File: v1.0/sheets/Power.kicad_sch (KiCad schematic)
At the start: 28 parts, among them U6 XC6206P152MR, U7 XC6206P282MR, U8 SY8088AAC

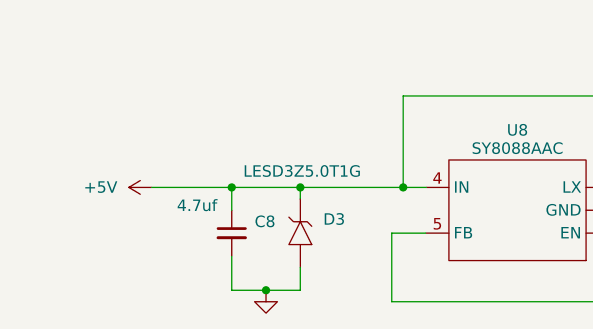
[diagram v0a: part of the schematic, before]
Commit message: V1.0 rework to match stm32u5xxxQ
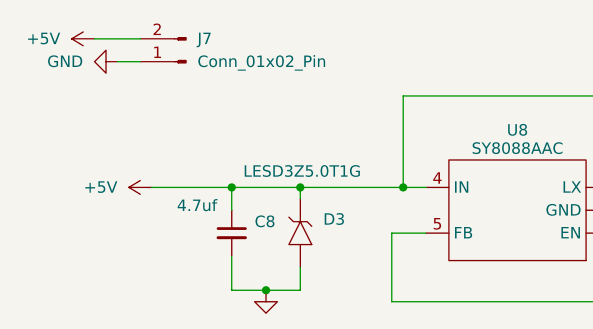
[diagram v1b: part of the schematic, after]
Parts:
- added J7: Conn_01x02_Pin, Connector_PinHeader_2.54mm:PinHeader_1x02_P2.54mm_Vertical, symbol Connector:Conn_01x02_Pin
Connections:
- net +5V: now also J7.2 (Pin_2)
- net GND: now also J7.1 (Pin_1)
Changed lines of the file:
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@@
 	(wire
 		(pts
+			(xy 17.78 15.24) (xy 22.86 15.24)
+		)
+		(stroke
+			(width 0)
+			(type default)
+		)
+	)
+	(wire
+		(pts
 			(xy 110.49 114.3) (xy 110.49 119.38)
 		)
@@
 	(wire
 		(pts
+			(xy 20.32 17.78) (xy 22.86 17.78)
+		)
+		(stroke
+			(width 0)
+			(type default)
+		)
+	)
+	(wire
+		(pts
 			(xy 24.13 31.75) (xy 33.02 31.75)
 		)
@@
 	)
 	(symbol
+		(lib_id "power:GND")
+		(at 20.32 17.78 270)
+		(unit 1)
+		(exclude_from_sim no)
+		(in_bom yes)
+		(on_board yes)
+		(dnp no)
+		(fields_autoplaced yes)
+		(property "Reference" "#PWR025"
+			(at 13.97 17.78 0)
+			(effects
+				(font
+					(size 1.27 1.27)
+				)
+				(hide yes)
+			)
+		)
+		(property "Value" "GND"
+			(at 16.51 17.7799 90)
+			(effects
+				(font
+					(size 1.27 1.27)
+				)
+				(justify right)
+			)
+		)
+		(property "Footprint" ""
+			(at 20.32 17.78 0)
+			(effects
+				(font
+					(size 1.27 1.27)
+				)
+				(hide yes)
+			)
+		)
+		(property "Datasheet" ""
+			(at 20.32 17.78 0)
+			(effects
+				(font
+					(size 1.27 1.27)
+				)
+				(hide yes)
+			)
+		)
+		(property "Description" "Power symbol creates a global label with name \"GND\" , ground"
+			(at 20.32 17.78 0)
+			(effects
+				(font
+					(size 1.27 1.27)
+				)
+				(hide yes)
+			)
+		)
+		(pin "1"
+		)
+		(instances
+			(project "v1.0"
+				(path "/4276d1e6-613e-409d-8b9b-79d391866e1c/7020a706-37b4-4081-90b2-84408c224fcc"
+					(reference "#PWR025")
+					(unit 1)
+				)
+			)
+		)
+	)
+	(symbol
 		(lib_id "Device:C_Small")
 		(at 121.92 36.83 0)
@@
 	)
 	(symbol
+		(lib_id "Connector:Conn_01x02_Pin")
+		(at 27.94 17.78 180)
+		(unit 1)
+		(exclude_from_sim no)
+		(in_bom yes)
+		(on_board yes)
+		(dnp no)
+		(fields_autoplaced yes)
+		(property "Reference" "J7"
+			(at 29.21 15.2399 0)
+			(effects
+				(font
+					(size 1.27 1.27)
+				)
+				(justify right)
+			)
+		)
+		(property "Value" "Conn_01x02_Pin"
+			(at 29.21 17.7799 0)
+			(effects
+				(font
+					(size 1.27 1.27)
+				)
+				(justify right)
+			)
+		)
+		(property "Footprint" "Connector_PinHeader_2.54mm:PinHeader_1x02_P2.54mm_Vertical"
+			(at 27.94 17.78 0)
+			(effects
+				(font
+					(size 1.27 1.27)
+				)
+				(hide yes)
+			)
+		)
+		(property "Datasheet" "~"
+			(at 27.94 17.78 0)
+			(effects
+				(font
+					(size 1.27 1.27)
+				)
+				(hide yes)
+			)
+		)
+		(property "Description" "Generic connector, single row, 01x02, script generated"
+			(at 27.94 17.78 0)
+			(effects
+				(font
+					(size 1.27 1.27)
+				)
+				(hide yes)
+			)
+		)
+		(pin "2"
+		)
+		(pin "1"
+		)
+		(instances
+			(project "v1.0"
+				(path "/4276d1e6-613e-409d-8b9b-79d391866e1c/7020a706-37b4-4081-90b2-84408c224fcc"
+					(reference "J7")
+					(unit 1)
+				)
+			)
+		)
+	)
+	(symbol
 		(lib_id "Grinreflex:MLF2012A1R5KT000")
 		(at 34.29 80.01 0)
@@
 					(unit 1)
 				)
+			)
+		)
+	)
+	(symbol
+		(lib_id "power:+5V")
+		(at 17.78 15.24 90)
+		(unit 1)
+		(exclude_from_sim no)
+		(in_bom yes)
+		(on_board yes)
+		(dnp no)
+		(fields_autoplaced yes)
+		(property "Reference" "#PWR074"
+			(at 21.59 15.24 0)
+			(effects
+				(font
+					(size 1.27 1.27)
+				)
+				(hide yes)
+			)
+		)
+		(property "Value" "+5V"
+			(at 13.97 15.2399 90)
+			(effects
+				(font
+					(size 1.27 1.27)
+				)
+				(justify left)
+			)
+		)
+		(property "Footprint" ""
+			(at 17.78 15.24 0)
+			(effects
+				(font
+					(size 1.27 1.27)
+				)
+				(hide yes)
+			)
+		)
+		(property "Datasheet" ""
+			(at 17.78 15.24 0)
+			(effects
+				(font
+					(size 1.27 1.27)
+				)
+				(hide yes)
+			)
+		)
+		(property "Description" "Power symbol creates a global label with name \"+5V\""
+			(at 17.78 15.24 0)
+			(effects
+				(font
+					(size 1.27 1.27)
+				)
+				(hide yes)
+			)
+		)
+		(pin "1"
+		)
+		(instances
+			(project "v1.0"
+				(path "/4276d1e6-613e-409d-8b9b-79d391866e1c/7020a706-37b4-4081-90b2-84408c224fcc"
+					(reference "#PWR074")
+					(unit 1)
+				)
